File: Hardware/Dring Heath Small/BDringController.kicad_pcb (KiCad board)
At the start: 4 copper layers, 144.8 x 131.4 mm, 93 parts, among them J1 Module 1, J10 Module 3, J11 JTAG, J12 Shift Regs and Motor Drvs, J13 Module 4, J14 Module 5, J15 Micro_SD_Card, J16 Pin, J17 Pin, J18 Pin, J19 Pin, J2 Jumper, J20 Pin, J21 Pin, J22 AUX GPIO, J3 Motor, J4 Module 1, J5 Ext Mot Drv, J6 01x02, J7 THC_Display, J8 Module 2, J9 VMot, U1 ESP32_38p, U10 Y, U11 z, U12 A, U13 B, U14 C, U2 74LVC157A, U3 ESP32_38p, U4 TC1262-33, U5 74AHCT595, U6 74AHCT595, U7 74AHCT595, U8 74AHCT595, U9 X

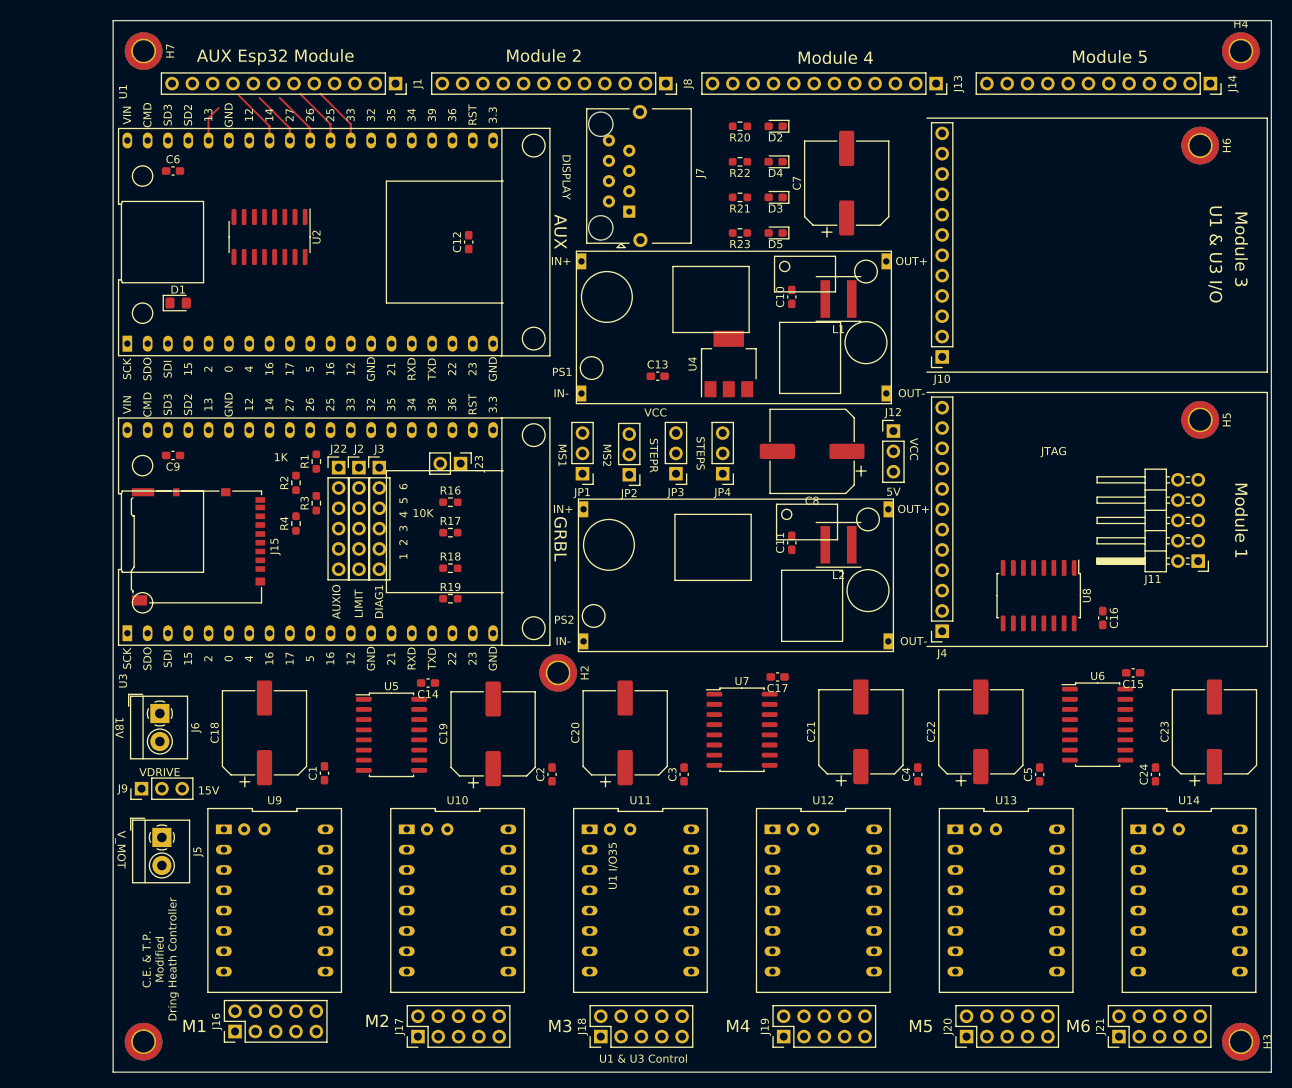
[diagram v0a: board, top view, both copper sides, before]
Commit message: Started routing main board
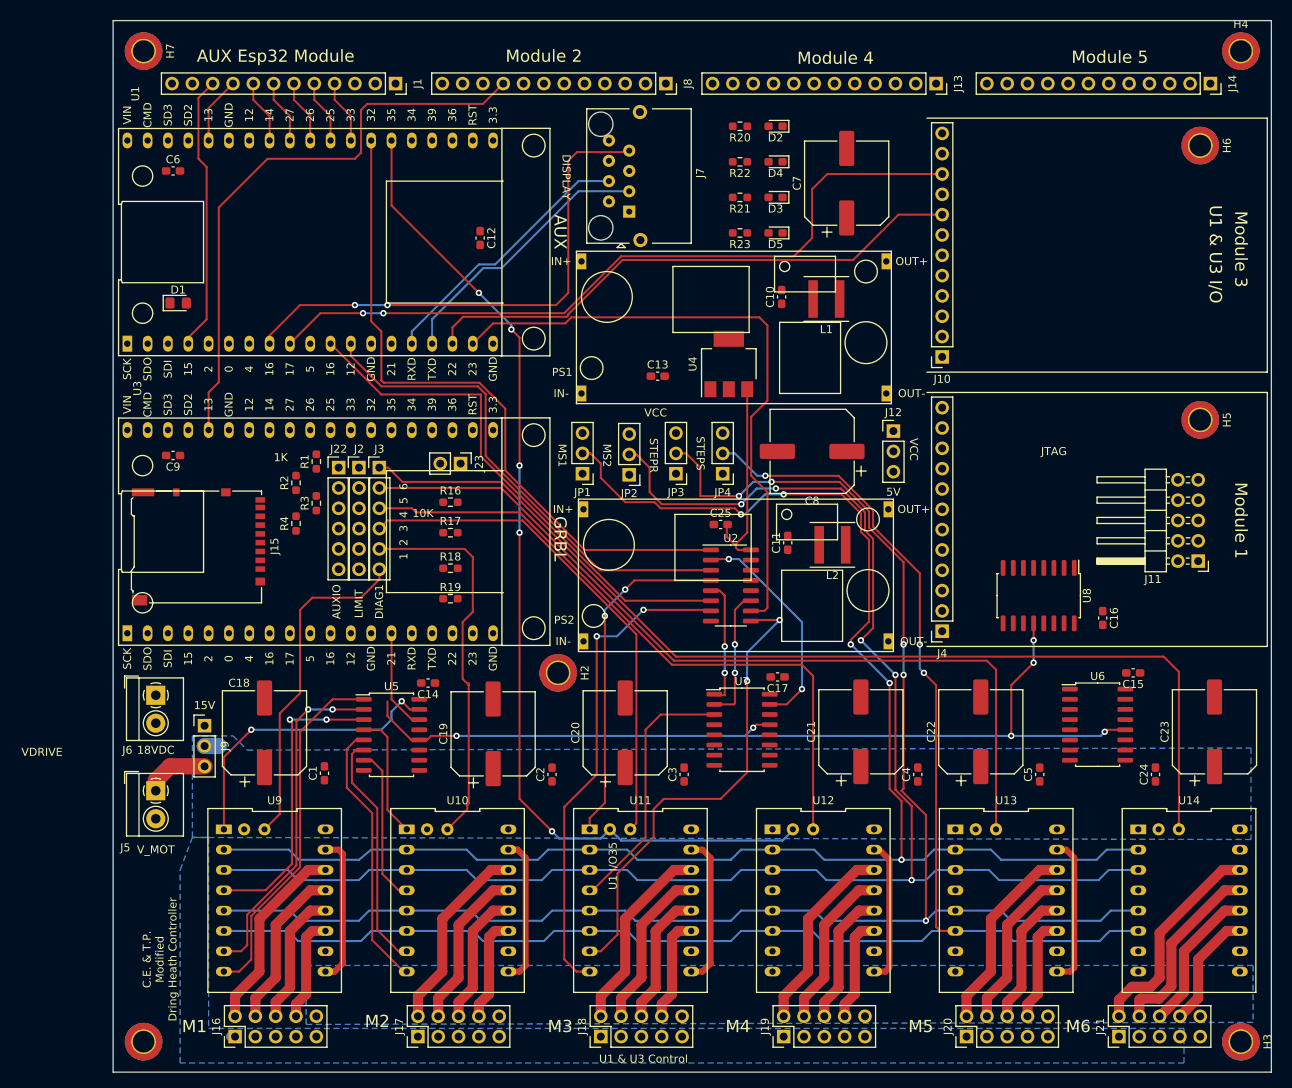
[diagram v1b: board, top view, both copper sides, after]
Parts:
- added C25: 100nf, Capacitor_SMD:C_0603_1608Metric_Pad1.08x0.95mm_HandSolder, F.Cu at (136.9, 88.4)
- moved U2 72.3 mm to (138.2, 96.0), turned to 0 degrees
- moved J9 11.1 mm to (72.4, 113.5), turned to 0 degrees
- moved J5 5.89 mm to (66.3, 121.7)
- moved J6 2.34 mm to (66.3, 109.7)
- moved L1 1.52 mm to (150.1, 60.2)
- moved C12 1.51 mm to (106.8, 52.6), turned to 270 degrees
- moved C10 1.27 mm to (144.5, 59.9)
- moved L2 0.76 mm to (150.9, 90.9)
- moved J16 0.64 mm to (76.2, 152.4)
- moved C11 0.51 mm to (145.3, 90.7)
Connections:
- U7 pad 1: GrbZDir -> GrbZEn
- U7 pad 10: VCC -> I2S_BCK
- U7 pad 11: I2S_BCK -> Net-(U7-Pad11)
- U7 pad 12: I2S_WS -> Net-(U7-Pad12)
- U7 pad 13: GND -> I2S_WS
- U7 pad 14: Net-(U5-Pad9) -> Net-(U7-Pad14)
- U7 pad 15: GrbZEn -> Net-(U7-Pad15)
- U7 pad 2: GrbZStep -> GrbZDir
- U7 pad 3: Z_CS -> GrbZStep
- U7 pad 4: A_Enable -> Z_CS
- U7 pad 5: A_Dir -> A_Enable
- U7 pad 6: A_Step -> A_Dir
- U7 pad 7: A_CS -> A_Step
- U7 pad 8: GND -> Net-(U7-Pad8)
- U7 pad 9: Net-(U6-Pad14) -> Net-(U7-Pad9)
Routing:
- net MS1: track 0.00 -> 207.8 mm, vias 0 -> 5
- net MS2: track 0.00 -> 205.1 mm, vias 0 -> 5
- net Step_R: track 0.00 -> 204.6 mm, vias 0 -> 5
- net Step_S: track 0.00 -> 199.3 mm, vias 0 -> 3
- net C_Diag1: track 0.00 -> 130.2 mm
- net TCHIO35: track 0.00 -> 126.8 mm, vias 0 -> 5
- net I2S_WS: track 0.00 -> 114.7 mm, vias 0 -> 6
- net B_Diag1: track 0.00 -> 106.4 mm
- net TCHIO17: track 0.00 -> 94.7 mm, vias 0 -> 2
- net GND: track 0.00 -> 92.7 mm
- net TorchTrigger: track 0.00 -> 85.1 mm
- net A_Diag1: track 0.00 -> 82.1 mm
- net Net-(U1-Pad18): track 0.00 -> 77.8 mm
- net GPIO13: track 0.00 -> 73.4 mm
- net TCHIO22: track 0.00 -> 69.2 mm
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- added copper zone on B.Cu, net GND
- added copper zone on B.Cu, net Vdrive
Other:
- net class 15v added: clearance 0.254, trace_width 1.27, via_dia 1.524, via_drill 0.762
- board text added: "18VDC"
- board text removed: "18V"

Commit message: more routing and added Dring large folder
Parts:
- moved J12 13.1 mm to (160.5, 63.8)
- moved D1 12.3 mm to (79.2, 53.8)
- moved C24 10.4 mm to (198.1, 127.5), turned to 270 degrees
- moved C5 9.51 mm to (182.1, 127.5), turned to 270 degrees
- moved C3 8.86 mm to (136.4, 127.5), turned to 270 degrees
- moved C1 8.78 mm to (90.9, 127.5), turned to 270 degrees
- moved C2 8.20 mm to (113.5, 127.5), turned to 270 degrees
- moved C4 8.20 mm to (159.3, 127.5), turned to 270 degrees
- moved R1 2.74 mm to (83.8, 79.5), turned to 180 degrees
- moved R3 2.62 mm to (83.8, 85.1), turned to 180 degrees
- moved C10 1.27 mm to (144.5, 58.7)
- moved R2 0.89 mm to (83.8, 82.3), turned to 180 degrees
- moved C17 0.76 mm to (143.3, 107.4)
- moved R4 0.38 mm to (83.8, 87.9), turned to 180 degrees
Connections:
- J6 pad 2: Net-(J6-Pad2) -> GND
- PS1 pad 2: Net-(J6-Pad2) -> GND
- PS2 pad 2: Net-(J6-Pad2) -> GND
- U7 pad 1: GrbZEn -> GrbZDir
- U7 pad 10: I2S_BCK -> VCC
- U7 pad 11: Net-(U7-Pad11) -> I2S_BCK
- U7 pad 12: Net-(U7-Pad12) -> I2S_WS
- U7 pad 13: I2S_WS -> GND
- U7 pad 14: Net-(U7-Pad14) -> Net-(U5-Pad9)
- U7 pad 15: Net-(U7-Pad15) -> GrbZEn
- U7 pad 2: GrbZDir -> GrbZStep
- U7 pad 3: GrbZStep -> Z_CS
- U7 pad 4: Z_CS -> A_Enable
- U7 pad 5: A_Enable -> A_Dir
- U7 pad 6: A_Dir -> A_Step
- U7 pad 7: A_Step -> A_CS
- U7 pad 8: Net-(U7-Pad8) -> GND
- U7 pad 9: Net-(U7-Pad9) -> Net-(U6-Pad14)
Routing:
- net GND: track 92.7 -> 480.1 mm, vias 0 -> 22
- net VCC: track 0.00 -> 260.9 mm, vias 0 -> 5
- net Vdrive: track 2.29 -> 257.4 mm, vias 0 -> 14
- net GPIO14: track 0.00 -> 143.4 mm, vias 0 -> 3
- net GPIO13: track 73.4 -> 210.2 mm, vias 0 -> 3
- net GPIO04: track 0.00 -> 136.3 mm
- net GPIO16: track 0.00 -> 134.9 mm, vias 0 -> 1
- net GPIO15: track 0.00 -> 132.2 mm, vias 0 -> 3
- net I2S_BCK: track 0.00 -> 126.6 mm, vias 0 -> 7
- net GPIO12: track 0.00 -> 124.3 mm, vias 0 -> 1
- net +5V: track 0.00 -> 116.6 mm, vias 0 -> 6
- net GPIO27: track 0.00 -> 98.6 mm, vias 0 -> 1
- net GPIO26: track 0.00 -> 89.3 mm
- net I2SO_24: track 0.00 -> 71.9 mm
- net I2SO_26: track 0.00 -> 63.4 mm
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
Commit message: more routing
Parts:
- moved C11 3.34 mm to (144.8, 87.4)
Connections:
- J7 pad 10: (no net) -> GND
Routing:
- net GND: track 480.1 -> 646.0 mm, vias 22 -> 29
- net GPIO2: track 0.00 -> 112.3 mm, vias 0 -> 8
- net Y_Limit: track 24.5 -> 111.2 mm, vias 0 -> 5
- net TCHIO21: track 0.00 -> 86.5 mm, vias 0 -> 5
- net TorchTrigger: track 85.1 -> 171.1 mm, vias 0 -> 1
- net X_Limit: track 29.6 -> 115.0 mm, vias 0 -> 3
- net Z_Limit: track 40.0 -> 113.2 mm, vias 2 -> 6
- net A_Limit: track 27.6 -> 100.7 mm, vias 3 -> 8
- net C_Limit: track 23.2 -> 91.8 mm, vias 1 -> 6
- net B_Limit: track 24.5 -> 91.6 mm, vias 3 -> 8
- net GPIO12: track 124.3 -> 190.7 mm, vias 1 -> 4
- net GPIO14: track 143.4 -> 209.8 mm, vias 3 -> 5
- net GPIO25: track 0.00 -> 63.6 mm, vias 0 -> 2
- net MISO: track 20.1 -> 74.1 mm, vias 1 -> 3
- net SCK: track 16.7 -> 67.4 mm, vias 1 -> 6
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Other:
- copper layers 4 -> 2

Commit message: Routing
needs 2 Jumper wires 18v in and 15v
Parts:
- moved J11 3.59 mm to (199.1, 90.4)
- moved C16 3.39 mm to (185.4, 96.8)
- moved C24 1.55 mm to (196.6, 127.3)
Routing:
- net VCC: track 272.6 -> 662.0 mm, vias 7 -> 24
- net GND: track 646.0 -> 997.9 mm, vias 29 -> 48
- net GPIO15: track 132.2 -> 238.1 mm, vias 3 -> 7
- net Vdrive: track 257.4 -> 350.1 mm, vias 14 -> 17
- net +3V3: track 98.3 -> 185.4 mm, vias 2 -> 9
- net +15V: track 25.8 -> 101.8 mm, vias 2 -> 11
- net IO27: track 7.95 -> 64.8 mm, vias 0 -> 1
- net IO26: track 7.95 -> 63.3 mm, vias 0 -> 1
- net EN: track 0.00 -> 51.8 mm, vias 0 -> 8
- net IO25: track 7.95 -> 52.9 mm, vias 0 -> 1
- net IO33: track 7.95 -> 52.9 mm, vias 0 -> 1
- net Net-(J6-Pad1): track 0.00 -> 40.1 mm, vias 0 -> 2
- net Vin: track 26.4 -> 59.4 mm
- net +5V: track 128.4 -> 153.2 mm, vias 6 -> 8
- net I2SO_24: track 71.9 -> 86.8 mm
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
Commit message: Main and Module Boards Routed
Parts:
- removed the J11 at (199.1, 90.4)
- added H10: ~, Connector_Pin:Pin_D0.9mm_L10.0mm_W2.4mm_FlatFork, F.Cu at (158.8, 83.3)
- added H9: ~, Connector_Pin:Pin_D0.9mm_L10.0mm_W2.4mm_FlatFork, F.Cu at (116.8, 78.2)
- added ~: ~, Connector_Pin:Pin_D0.9mm_L10.0mm_W2.4mm_FlatFork, F.Cu at (64.0, 105.7)
- added ~: ~, Connector_Pin:Pin_D0.9mm_L10.0mm_W2.4mm_FlatFork, F.Cu at (72.4, 107.2)
- renumbered C6 to C1, C14 to C10, C15 to C11, C16 to C12, C17 to C13, C18 to C14, C1 to C15, C19 to C16, C2 to C17, C20 to C18, C3 to C19, C25 to C2, C21 to C20, C4 to C21, C5 to C23, C23 to C24, C24 to C25, C7 to C3, C8 to C4, C9 to C5, C10 to C6, C11 to C7, C12 to C8, C13 to C9, J22 to J1, J8 to J10, J9 to J11, J10 to J12, J12 to J13, J13 to J14, J14 to J15, J15 to J16, J16 to J17, J17 to J18, J18 to J19, J23 to J2, J19 to J20, J20 to J21, J21 to J22, J1 to J3, J2 to J4, J3 to J5, J4 to J6, J5 to J7, J6 to J8, J7 to J9, R21 to R10, R22 to R11, R23 to R12, R16 to R5, R17 to R6, R18 to R7, R19 to R8, R20 to R9
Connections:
- J9 pad 9: (no net) -> GND
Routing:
- net GND: track 997.9 -> 1015.5 mm, vias 48 -> 51
- net Net-(J6-Pad1): track 0.00 -> 5.01 mm
- net Net-(H9-Pad1): track 40.1 -> 35.0 mm, vias 2 -> 0
- net +15V: vias 11 -> 9
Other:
- board text removed: "JTAG"

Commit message: Pin changes
Put RJ45 connector on Jtag module for more IO put Pot on Torch module to
adjust Plasma voltage
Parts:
- renumbered ~ to H11, ~ to H8
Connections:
- J12 pad 10: TCHIO17 -> TCH_V_IO36
- J9 pad 10: GND -> (no net)
- J9 pad 9: GND -> (no net)
- U1 pad 22: Net-(U1-Pad22) -> TCH_V_IO36
- U1 pad 9: TCHIO17 -> Net-(U1-Pad9)
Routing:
- net TCHIO17: track 98.7 -> 0.00 mm, vias 2 -> 0
- net TCH_V_IO36: track 0.00 -> 72.2 mm, vias 0 -> 3

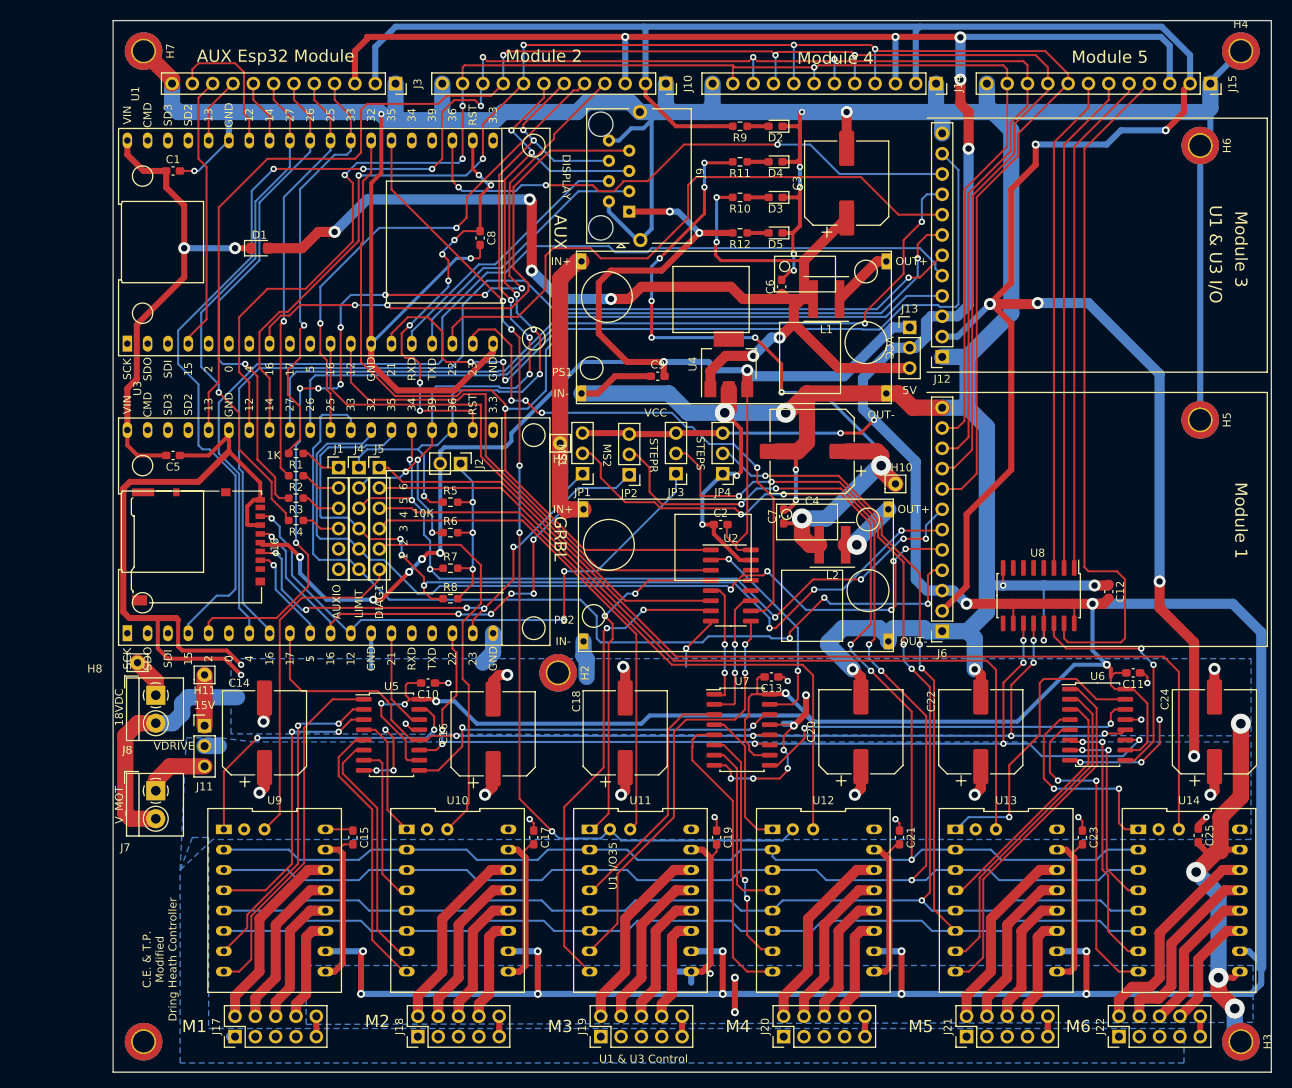
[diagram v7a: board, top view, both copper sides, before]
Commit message: Change to BOM
Shifted a few tracks changed 3.3v reg to 1A
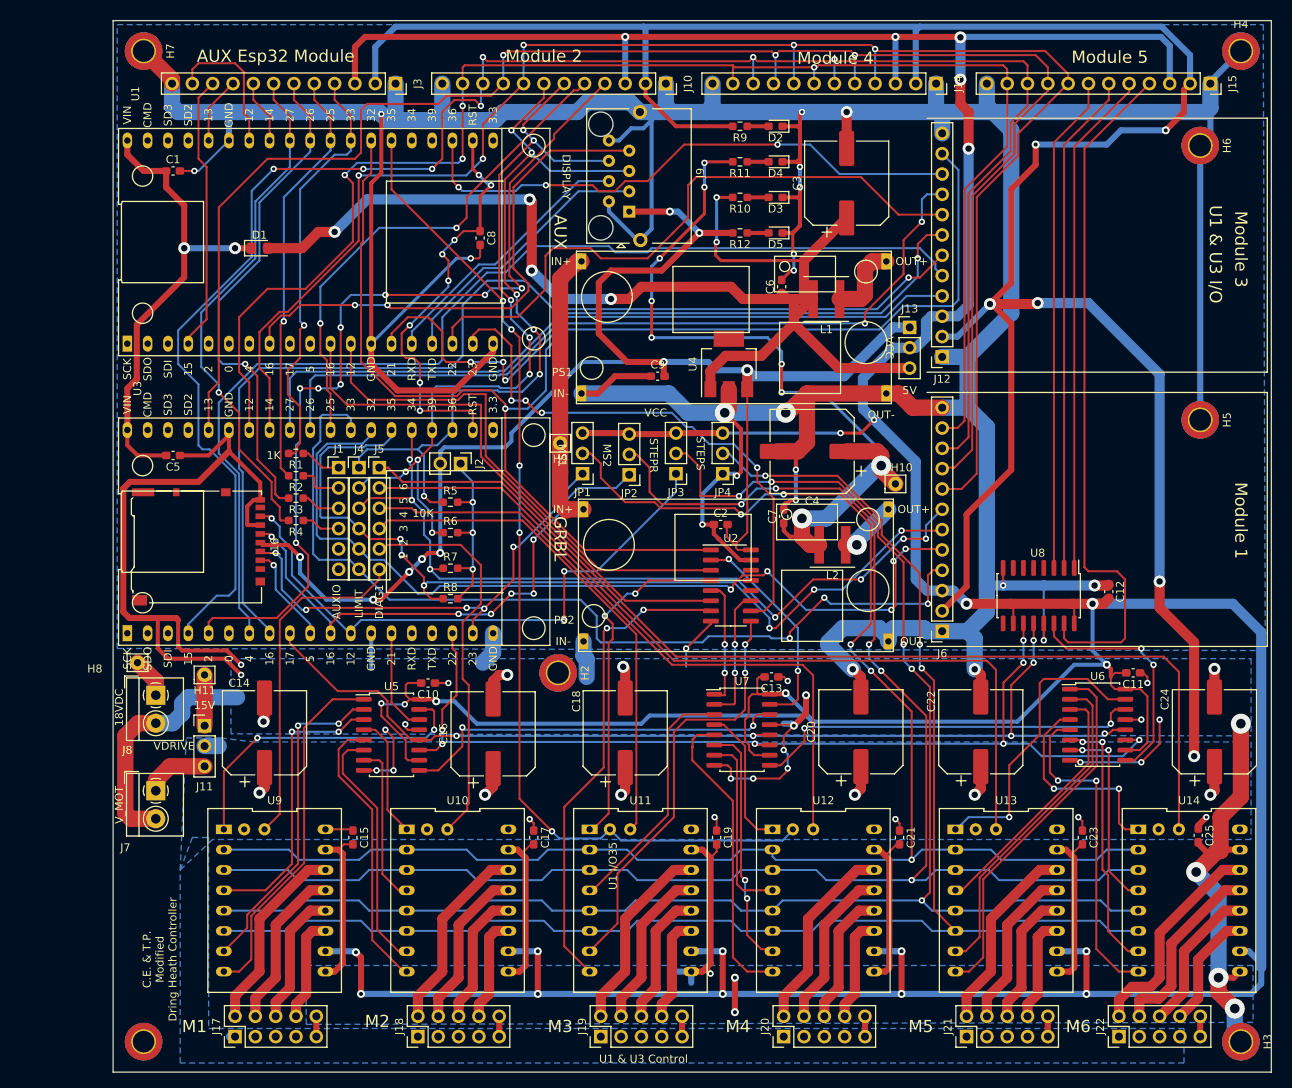
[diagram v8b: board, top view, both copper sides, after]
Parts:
- U4: value TC1262-33 -> BL8071CLATR33
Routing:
- net +5V: track 153.2 -> 156.2 mm, vias 8 -> 6
- net +15V: track 101.8 -> 104.7 mm
- net I2S_WS: track 132.3 -> 129.7 mm
- net Net-(L1-Pad1): track 7.78 -> 9.72 mm
- net Net-(J1-Pad2): track 5.05 -> 6.01 mm
- net TCH_V_IO36: track 72.2 -> 71.4 mm
- net B_Dir: track 45.6 -> 46.4 mm
- net IO33: track 52.9 -> 53.6 mm
- net A_Step: track 30.2 -> 30.8 mm
- net B_Step: track 41.1 -> 41.7 mm
- net A_CS: track 22.7 -> 23.3 mm
- net Y_Dir: track 34.6 -> 35.2 mm
- net Y_Step: track 30.7 -> 31.3 mm
- net B_CS: track 31.5 -> 32.1 mm
- net TorchTrigger: track 173.0 -> 172.5 mm
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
